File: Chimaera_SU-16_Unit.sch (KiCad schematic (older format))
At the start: 63 parts, among them P0 CONN_4, P1 CONN_4, P2 CONN_3, U0 CD74HC4067, U1 MCP602, U2 MCP1703

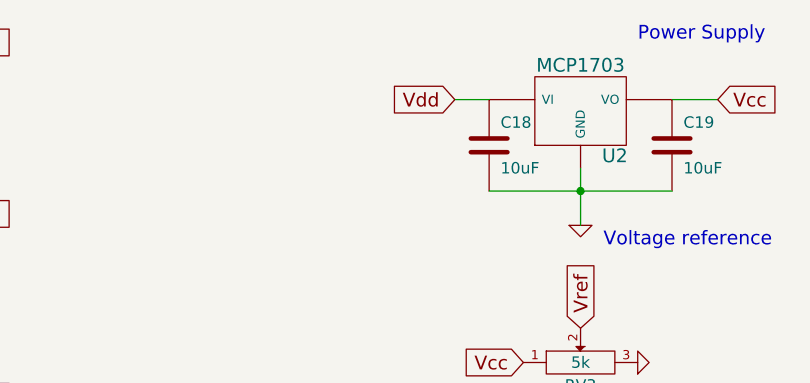
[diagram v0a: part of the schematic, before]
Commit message: DSP-F3 rev3 (+1 analog input) and SU-16 rev7 (reverse current diode), Hershey fonts for case side
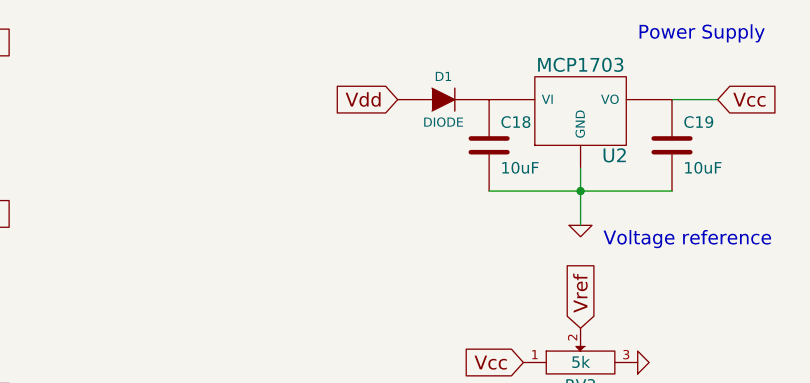
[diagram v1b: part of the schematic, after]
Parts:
- added D1: DIODE, ~, symbol DIODE
- U2: Digi-Key (none) -> MCP1703-5002E/DB-ND
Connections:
- net Vdd: now also D1.1 (A); no longer C18.1, U2.1 (VI)
- new net: C18.1, D1.2 (K), U2.1 (VI)
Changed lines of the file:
@@
 LIBS:lm1117
 LIBS:MCP602
+LIBS:Chimaera_SU-16_Unit-cache
 EELAYER 27 0
 EELAYER END
@@
 encoding utf-8
 Sheet 1 1
-Title "Chimaera Sensor Unit"
-Date "18 jul 2013"
-Rev "4"
-Comp "Open Music Kontrollers (Hanspeter Portner)"
+Title "Chimaera Sensor Unit (SU-16)"
+Date "13 aug 2013"
+Rev "7"
+Comp "Open Music Kontrollers (www.open-music-kontrollers.ch)"
 Comment1 "Licensed under CERN OHL v.1.1"
-Comment2 ""
+Comment2 "Copyright (c) 2013 Hanspeter Portner (dev@open-music-kontrollers.ch)"
 Comment3 ""
 Comment4 ""
@@
 Text GLabel 5050 3050 0    60   Input ~ 0
 Ain
-Text GLabel 5400 850  0    60   Input ~ 0
+Text GLabel 5150 850  0    60   Input ~ 0
 Vdd
 Text GLabel 6550 850  2    60   Input ~ 0
@@
 F 2 "" H 5950 900 60  0001 C CNN
 F 3 "" H 5950 900 60  0001 C CNN
+F 4 "MCP1703-5002E/DB-ND" H 5950 900 60  0001 C CNN "Digi-Key"
 	1    5950 900
 	1    0    0    -1
@@
 	6350 850  6550 850
 Wire Wire Line
-	5400 850  5550 850
-Wire Wire Line
 	6800 7500 6800 7350
 Wire Wire Line
@@
 	6550 7050 6550 7350
 Connection ~ 5800 7050
+$Comp
+L DIODE D1
+U 1 1 5209E981
+P 5350 850
+F 0 "D1" H 5350 950 40  0000 C CNN
+F 1 "DIODE" H 5350 750 40  0000 C CNN
+F 2 "~" H 5350 850 60  0000 C CNN
+F 3 "~" H 5350 850 60  0000 C CNN
+	1    5350 850
+	1    0    0    -1
+$EndComp
 $EndSCHEMATC

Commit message: last changes for Alpha Batch PCBs
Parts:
- added C37: 1uF, ~, symbol C
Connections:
- net GND: now also C37.1
- net Vcc: now also C37.2
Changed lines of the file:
@@
 Sheet 1 1
 Title "Chimaera Sensor Unit (SU-16)"
-Date "13 aug 2013"
+Date "16 aug 2013"
 Rev "7"
 Comp "Open Music Kontrollers (www.open-music-kontrollers.ch)"
@@
 	1    0    0    -1
 $EndComp
+$Comp
+L C C37
+U 1 1 520DF67B
+P 6550 2850
+F 0 "C37" H 6550 2950 40  0000 L CNN
+F 1 "1uF" H 6556 2765 40  0000 L CNN
+F 2 "~" H 6588 2700 30  0000 C CNN
+F 3 "~" H 6550 2850 60  0000 C CNN
+	1    6550 2850
+	1    0    0    -1
+$EndComp
+Wire Wire Line
+	6550 2650 6700 2650
 $EndSCHEMATC

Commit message: EDA: add missing Digi-Key part numbers
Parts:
- C0, C1, C10, C11, C12, C13, C14, C15, C16, C17, C2, C3, C4, C5, C6, C7, C8, C9: Digi-Key (none) -> 445-1316-1-ND
- C18, C19: Digi-Key (none) -> 445-4042-1-ND
- C20, C21, C22, C23, C24, C25, C26, C27, C28, C29, C30, C31, C32, C33, C34, C35, C36, C37: Digi-Key (none) -> 445-1358-1-ND
- D1: Digi-Key (none) -> 568-6512-1-ND
- P1: Digi-Key (none) -> S5479-ND
- R1: Digi-Key (none) -> P20KACT-ND
- RV1: Digi-Key (none) -> ST4ETB204CT-ND
- RV2, RV3: Digi-Key (none) -> ST4ETB502CT-ND
- S0, S1, S10, S11, S12, S13, S14, S15, S2, S3, S4, S5, S6, S7, S8, S9: Digi-Key (none) -> 620-1019-1-ND
- U0: Digi-Key (none) -> 296-9225-5-ND
- U1: Digi-Key (none) -> MCP602-I/SN-ND
